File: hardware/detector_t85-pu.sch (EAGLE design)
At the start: 40 parts, among them J1 AVR_SPI_PRG_6NS, Q1 BS170, Q2 16MHz, T1 BC337, T2 BC337, U1 TINY85-20-DIP

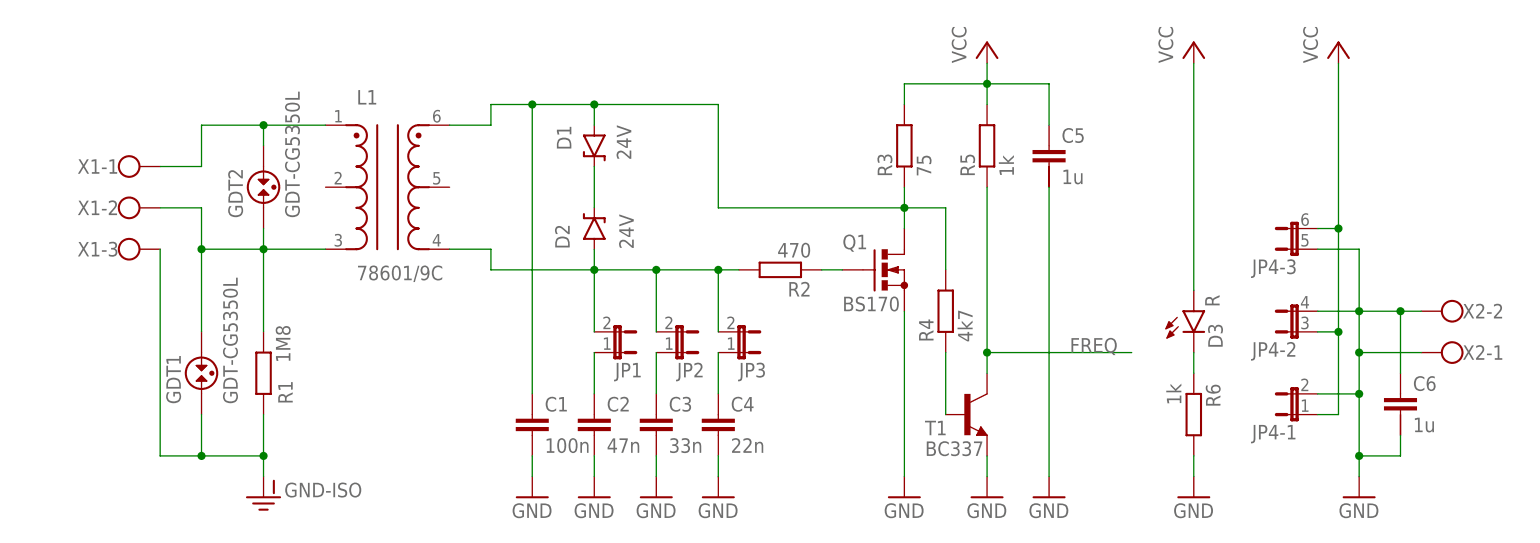
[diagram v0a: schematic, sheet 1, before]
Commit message: hardware: t85 all parts on the board
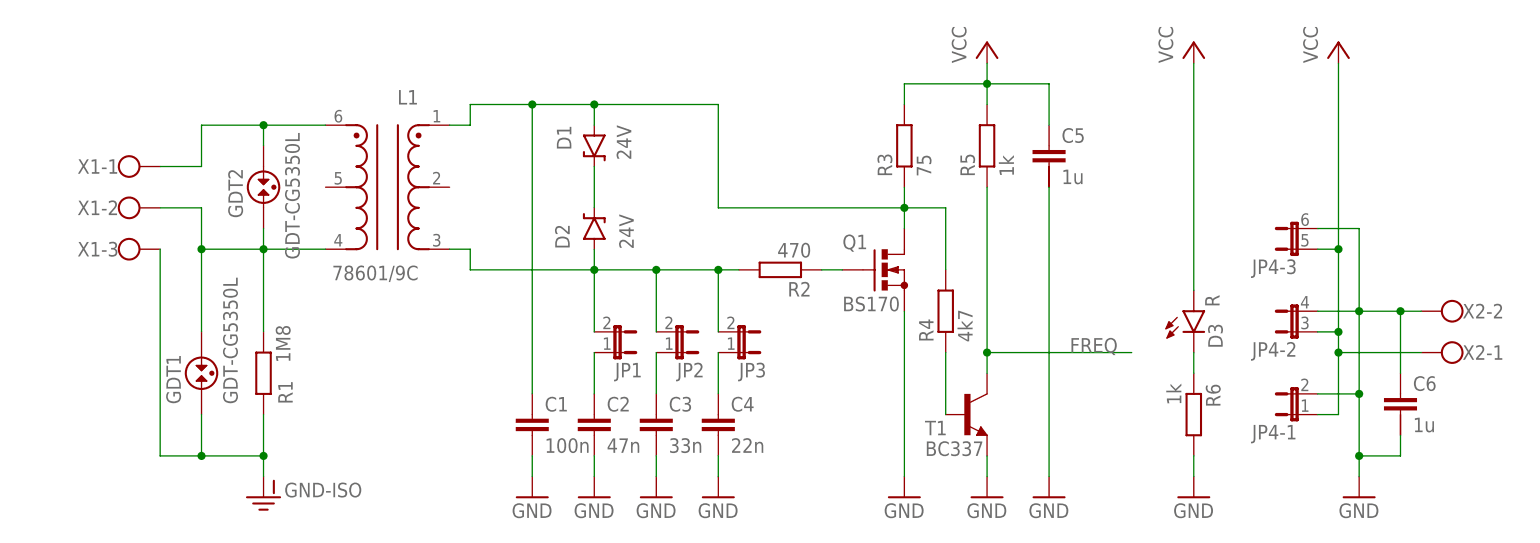
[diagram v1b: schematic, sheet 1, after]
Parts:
- C7, C8: device resistor:C-EU050-024X044 -> SparkFun-Capacitors:CAPPTH2
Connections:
- net GND: now also JP4-3.2; no longer JP4-3.1, X2-1.KL
- net N$14: now also L1.1; no longer L1.6
- net N$21: now also L1.4; no longer L1.3
- net N$6: now also L1.3; no longer L1.4
- net N$7: now also L1.6; no longer L1.1
- net VCC: now also JP4-3.1, X2-1.KL; no longer JP4-3.2

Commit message: hardware: t85 board fuckery
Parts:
- added C9: 1u, rcl:C-EU050-025X075
- C5, C6: device capacitor-wima:C-2.5-5/4 -> rcl:C-EU050-025X075
- Q1: value BS170 -> BS170.; device transistor-small-signal:BS170 -> detector:BS170.
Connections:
- net GND: now also C9.2; no longer C6.1
- net GND-ISO: now also X1-2.KL; no longer X1-3.KL
- net N$21: now also L1.6, X1-3.KL; no longer L1.4, X1-2.KL
- net N$7: now also L1.4; no longer L1.6
- net VCC: now also C6.1, C9.1
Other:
- moved on the sheet: GDT1, GDT2, L1, R1, X1-1, X1-2, X1-3

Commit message: hardware-t85: almost there
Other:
- moved on the sheet: C5, C7, C8, C9, D4, D5, J1, JP5, Q2, R10, R11, R7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

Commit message: hardware-t85: really almost there
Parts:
- D1, D2: device SparkFun-DiscreteSemi:DIODE-ZENER -> diode:ZENER-DIODEZD-5
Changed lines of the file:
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@@
 <part name="R3" library="resistor" deviceset="R-EU_" device="0204/7" value="75"/>
 <part name="GND6" library="supply1" deviceset="GND" device=""/>
-<part name="D1" library="SparkFun-DiscreteSemi" deviceset="DIODE-ZENER" device="" value="24V"/>
-<part name="D2" library="SparkFun-DiscreteSemi" deviceset="DIODE-ZENER" device="" value="24V"/>
+<part name="D1" library="diode" deviceset="ZENER-DIODE" device="ZD-5" value="24V"/>
+<part name="D2" library="diode" deviceset="ZENER-DIODE" device="ZD-5" value="24V"/>
 <part name="GND-ISO1" library="SparkFun-Aesthetics" deviceset="GND-ISO" device=""/>
 <part name="R1" library="resistor" deviceset="R-EU_" device="0204/5" value="1M8"/>
@@
 <instance part="D1" gate="G$1" x="73.66" y="53.34" smashed="yes" rot="R270">
 <attribute name="NAME" x="69.0626" y="55.88" size="1.778" layer="95" rot="R270"/>
-<attribute name="VALUE" x="76.4286" y="55.88" size="1.778" layer="96" rot="R270"/>
 </instance>
 <instance part="D2" gate="G$1" x="73.66" y="43.18" smashed="yes" rot="R90">
 <attribute name="NAME" x="70.6374" y="40.64" size="1.778" layer="95" rot="R90"/>
-<attribute name="VALUE" x="78.5114" y="40.64" size="1.778" layer="96" rot="R90"/>
 </instance>
 <instance part="GND-ISO1" gate="G$1" x="30.48" y="10.16"/>
